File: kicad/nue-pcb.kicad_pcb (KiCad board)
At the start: 2 copper layers, 293.9 x 103.4 mm, 154 parts, among them J1 Conn_01x04, J2 AVR-ISP-6, SW1 ESC, SW10 9, SW101 FN1, SW102 SPACE2.75, SW103 SPACE2.25, SW11 0, SW12 -, SW13 =, SW14 2U BACKSP, SW15 TAB150, SW16 Q, SW17 W, SW18 E, SW19 R, SW2 1, SW20 T, SW21 Y, SW22 U, SW23 I, SW24 O, SW25 P, SW26 CURL_L, SW27 CURL_R, SW28 1U RBKSP, SW29 CAPS, SW3 2, SW30 A, SW31 S, SW32 D, SW33 F, SW34 G, SW35 H, SW36 J, SW37 K, SW38 L, SW39 ;, SW4 3, SW40 ', SW41 PIPE150, SW42 ENTER_ANSI, SW43 LSHIFT225, SW44 ISO_PIPE, SW45 Z, SW46 X, SW47 C, SW48 V, SW49 B, SW5 4, SW50 N, SW51 M, SW52 <, SW53 >, SW54 ?, SW55 RSHIFT275, SW56 FN, SW6 5, SW61 FN2, SW65 1U LBACKSP, SW66 STEPPEDCAPS, SW69 RSHIFT175, SW7 6, SW70 LCTRL150, SW71 LWIN100, SW72 LALT150, SW73 SPACE700, SW74 RALT150, SW75 RWIN100, SW76 RCTRL150, SW8 7, SW9 8, U1 ATmega32U4-MU, Y1 16 MHz

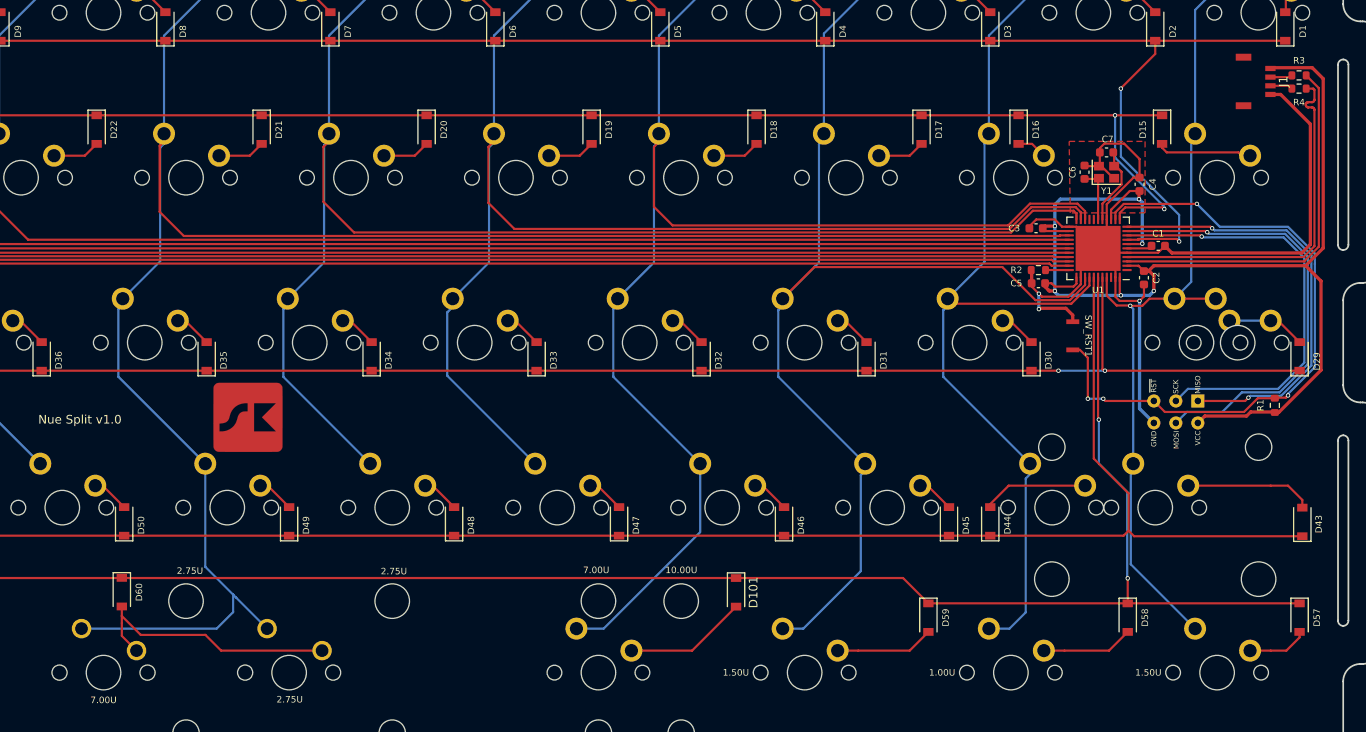
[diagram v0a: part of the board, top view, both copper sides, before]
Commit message: replace jst footprint, make 2.75/7/10u holes smaller
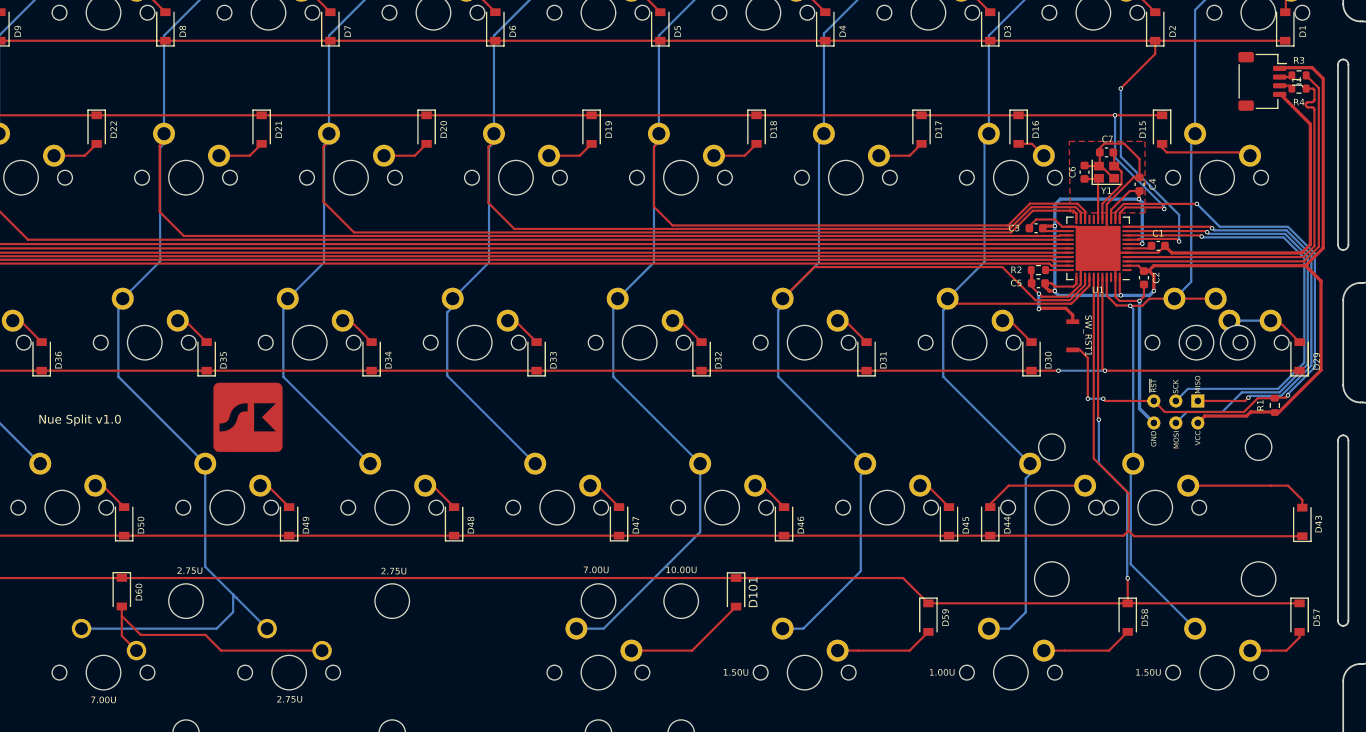
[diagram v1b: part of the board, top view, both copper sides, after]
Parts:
- J1: footprint kestralib:JST_BM04B-ASRS -> Connector_JST:JST_SH_SM04B-SRSS-TB_1x04-1MP_P1.00mm_Horizontal
- SW102: footprint kestralib:MXOnly-2.75U-ReversedStabilizers-NoLED -> kestralib:MX275R
- SW73: footprint kestralib:MXOnly-10U-7U-ReversedStabilizers-NoLED -> kestralib:MX10-7U
- moved J1 0.33 mm to (332.3, 73.0)
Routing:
- net VCC: track 140.3 -> 139.2 mm
- net Net-(J1-Pad2): track 2.56 -> 1.49 mm
- net GND: track 125.9 -> 124.9 mm
- net Net-(J1-Pad3): track 2.62 -> 1.55 mm
